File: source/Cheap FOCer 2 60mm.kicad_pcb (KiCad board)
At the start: 2 copper layers, 59.1 x 99.9 mm, 228 parts, among them J1 Conn_01x02, J2 Conn_01x07, J3 Conn_01x03, J4 On/Off, J5 UNUSED MCU PINS, J6 Conn_01x03, P1 MOTOR1, P2 MOTOR1, P3 MOTOR1, P4 HALL/Encoder, P5 SWD, Q1 NCEP60T20, Q10 Q_PNP_BCE, Q11 Q_PNP_BCE, Q12 Q_PNP_BCE, Q2 NCEP60T20, Q3 NCEP60T20, Q4 NCEP60T20, Q5 NCEP60T20, Q6 NCEP60T20, Q7 Q_PNP_BCE, Q8 Q_PNP_BCE, Q9 Q_PNP_BCE, U1 AMS1117-3.3, U2 DRV8301, U3 TP2604-SR, U4 TJA1051T/3/1J, U5 STM32F405RGT6, U6 BMI160, X1 8MHz 10ppm (X50328MSB2GI)

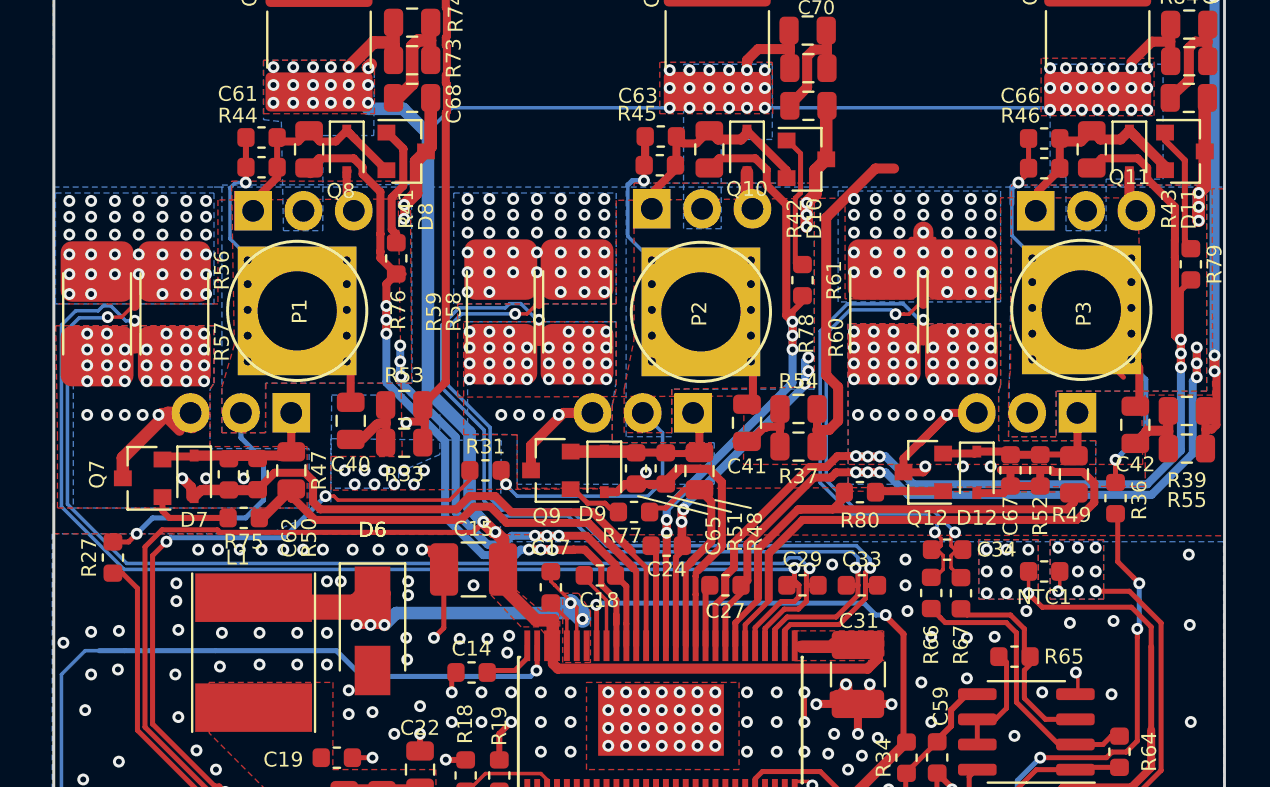
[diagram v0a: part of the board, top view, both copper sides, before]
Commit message: Removed gate transistors
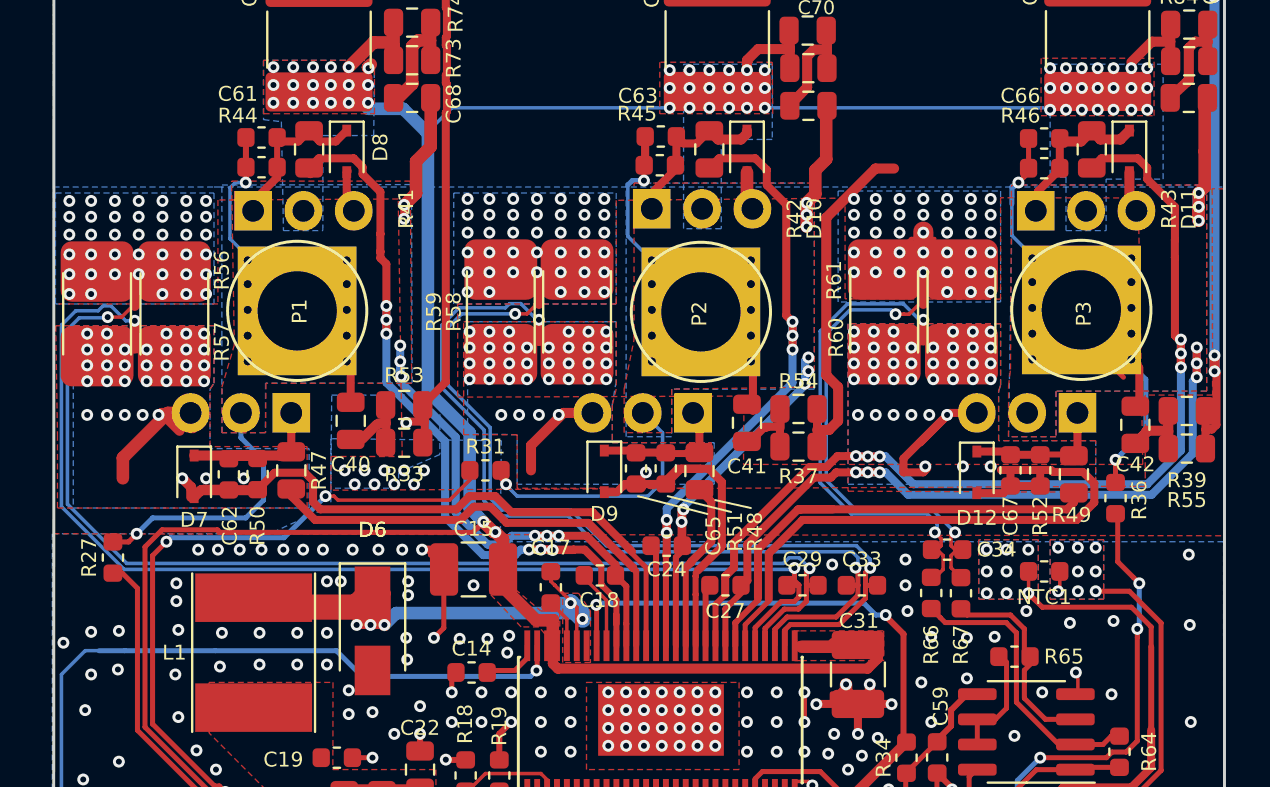
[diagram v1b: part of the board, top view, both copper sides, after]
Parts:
- removed Q10, Q11, Q12, Q7, Q8, Q9: Q_PNP_BCE, Package_TO_SOT_SMD:SOT-23
- removed R75, R76, R77, R78, R79, R80: 4.7R, Resistor_SMD:R_0603_1608Metric
- R41, R42, R43, R47, R48, R49: value 4.7R -> 10R
- R56, R57, R58, R59, R60, R61: value 0.002R -> 0.001R
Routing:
- net Net-(Q10-Pad1): track 7.33 -> 0.00 mm
- net Net-(Q11-Pad1): track 6.73 -> 0.00 mm
- net Net-(Q8-Pad1): track 6.63 -> 0.00 mm
- net Net-(Q7-Pad1): track 4.16 -> 0.00 mm
- net Net-(C61-Pad1): track 14.1 -> 10.4 mm
- net /Mosfet driver/GH_C: track 58.0 -> 54.3 mm
- net Net-(Q12-Pad1): track 3.60 -> 0.00 mm
- net Net-(C66-Pad1): track 12.8 -> 9.52 mm
- net Net-(C65-Pad1): track 13.1 -> 9.83 mm
- net Net-(C63-Pad1): track 13.3 -> 10.1 mm
- net /Mosfet driver/GL_B: track 12.0 -> 9.06 mm
- net Net-(Q9-Pad1): track 2.81 -> 0.00 mm
- net Net-(C62-Pad1): track 14.6 -> 12.0 mm
- net /Mosfet driver/GL_A: track 26.0 -> 23.7 mm
- net Net-(C67-Pad1): track 8.97 -> 7.23 mm
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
